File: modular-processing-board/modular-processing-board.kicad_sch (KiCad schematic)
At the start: 0 parts

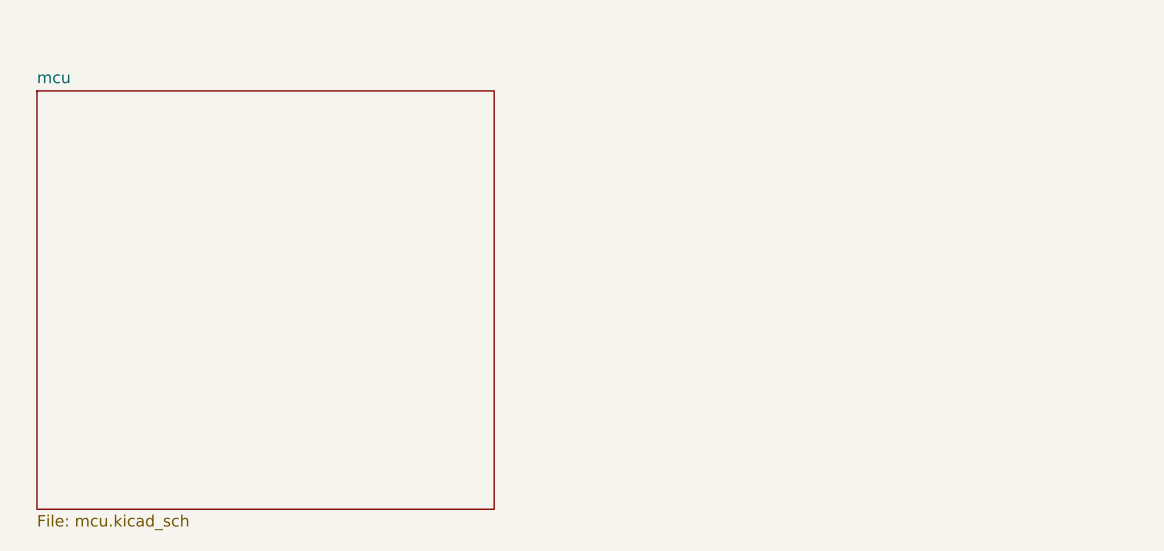
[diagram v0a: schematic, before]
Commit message: research on best communication interfaces, added sdram
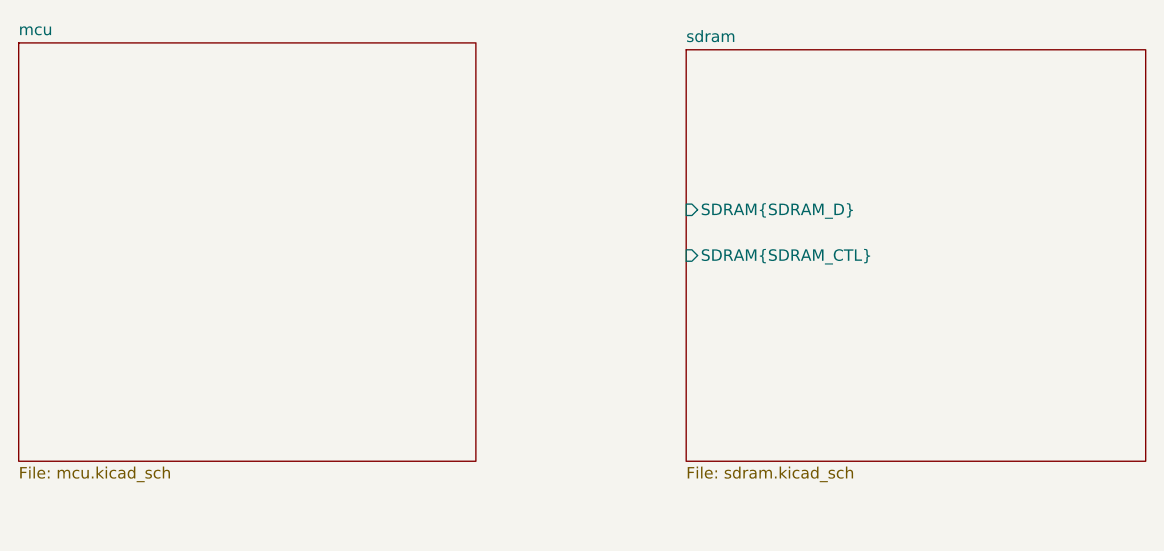
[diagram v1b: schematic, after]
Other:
- added sheet sdram (sdram.kicad_sch)
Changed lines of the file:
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@@
 	(paper "A4")
 	(sheet
-		(at 51.308 64.262)
+		(at 49.276 58.928)
 		(size 50.8 46.482)
 		(exclude_from_sim no)
@@
 		)
 		(property "Sheetname" "mcu"
-			(at 51.308 63.5504 0)
+			(at 49.276 58.2164 0)
 			(effects
 				(font
@@
 		)
 		(property "Sheetfile" "mcu.kicad_sch"
-			(at 51.308 111.3286 0)
+			(at 49.276 105.9946 0)
 			(effects
 				(font
@@
 				)
 			)
+		)
+	)
+	(sheet
+		(at 123.444 59.69)
+		(size 51.054 45.72)
+		(exclude_from_sim no)
+		(in_bom yes)
+		(on_board yes)
+		(dnp no)
+		(fields_autoplaced yes)
+		(stroke
+			(width 0.1524)
+			(type solid)
+		)
+		(fill
+			(color 0 0 0 0.0000)
+		)
+		(property "Sheetname" "sdram"
+			(at 123.444 58.9784 0)
+			(effects
+				(font
+					(size 1.27 1.27)
+				)
+				(justify left bottom)
+			)
+		)
+		(property "Sheetfile" "sdram.kicad_sch"
+			(at 123.444 105.9946 0)
+			(effects
+				(font
+					(size 1.27 1.27)
+				)
+				(justify left top)
+			)
+		)
+		(pin "SDRAM{SDRAM_D}" input
+			(at 123.444 77.47 180)
+			(effects
+				(font
+					(size 1.27 1.27)
+				)
+				(justify left)
+			)
+		)
+		(pin "SDRAM{SDRAM_CTL}" input
+			(at 123.444 82.55 180)
+			(effects
+				(font
+					(size 1.27 1.27)
+				)
+				(justify left)
+			)
+		)
+		(instances
+			(project "modular-processing-board"
+				(path "/73b5a92f-908b-4f97-a96c-14ee20a7f293"
+					(page "3")
+				)
+			)

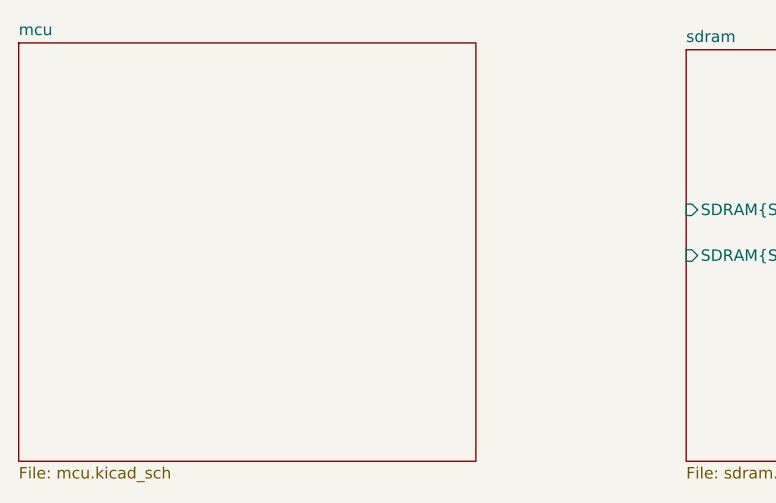
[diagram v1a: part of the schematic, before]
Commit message: basicsic pinout/component selection done, added SDRAM pins (next) Add parallel pins, add connections to pinheaders
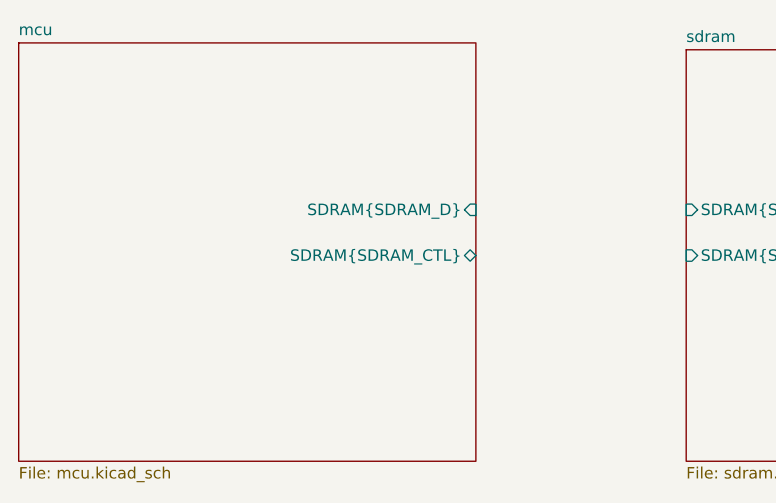
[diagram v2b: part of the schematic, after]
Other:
- sheet mcu ports: added SDRAM{SDRAM_CTL}, SDRAM{SDRAM_D}; removed none
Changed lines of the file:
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@@
+			)
+		)
+		(pin "SDRAM{SDRAM_CTL}" bidirectional
+			(at 100.076 82.55 0)
+			(effects
+				(font
+					(size 1.27 1.27)
+				)
+				(justify right)
+			)
+		)
+		(pin "SDRAM{SDRAM_D}" input
+			(at 100.076 77.47 0)
+			(effects
+				(font
+					(size 1.27 1.27)
+				)
+				(justify right)
 			)
 		)

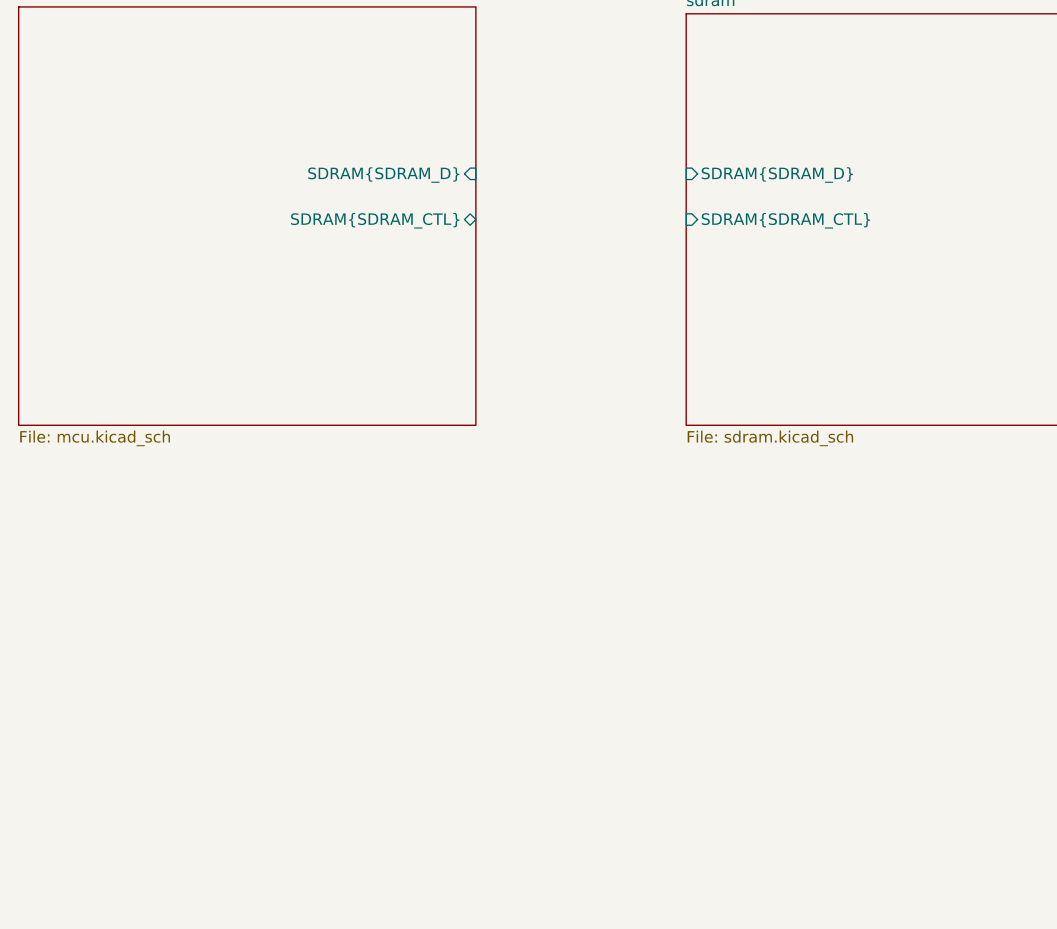
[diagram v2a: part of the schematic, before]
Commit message: added parallel slave bus, SWO, USB (next) add small PSU for CPU-board, add ethernet PHY, add correct USB connector
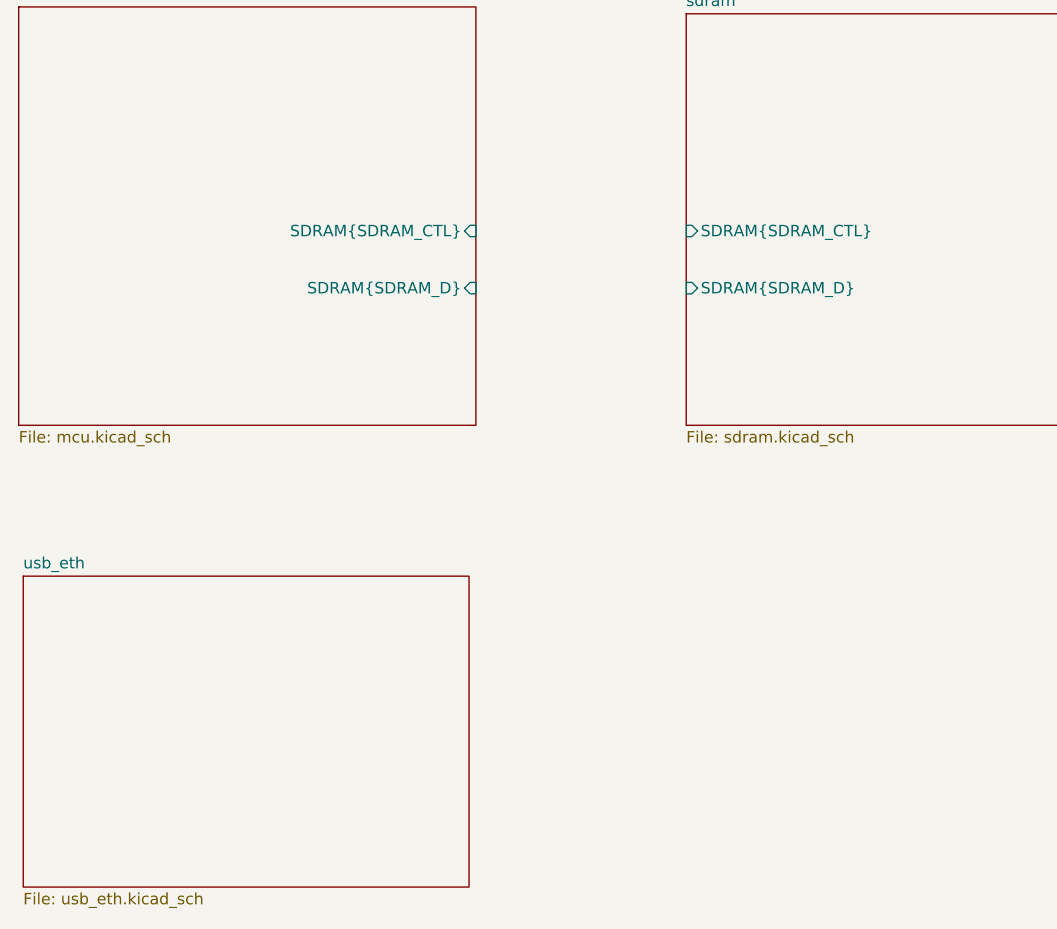
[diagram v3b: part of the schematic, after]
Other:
- added sheet usb_eth (usb_eth.kicad_sch)
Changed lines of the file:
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@@
 			)
 		)
-		(pin "SDRAM{SDRAM_CTL}" bidirectional
-			(at 100.076 82.55 0)
+		(pin "SDRAM{SDRAM_D}" input
+			(at 100.076 90.17 0)
 			(effects
 				(font
@@
 			)
 		)
-		(pin "SDRAM{SDRAM_D}" input
-			(at 100.076 77.47 0)
+		(pin "SDRAM{SDRAM_CTL}" input
+			(at 100.076 83.82 0)
 			(effects
 				(font
@@
 				(path "/73b5a92f-908b-4f97-a96c-14ee20a7f293"
 					(page "2")
+				)
+			)
+		)
+	)
+	(sheet
+		(at 49.784 122.174)
+		(size 49.53 34.544)
+		(exclude_from_sim no)
+		(in_bom yes)
+		(on_board yes)
+		(dnp no)
+		(fields_autoplaced yes)
+		(stroke
+			(width 0.1524)
+			(type solid)
+		)
+		(fill
+			(color 0 0 0 0.0000)
+		)
+		(property "Sheetname" "usb_eth"
+			(at 49.784 121.4624 0)
+			(effects
+				(font
+					(size 1.27 1.27)
+				)
+				(justify left bottom)
+			)
+		)
+		(property "Sheetfile" "usb_eth.kicad_sch"
+			(at 49.784 157.3026 0)
+			(effects
+				(font
+					(size 1.27 1.27)
+				)
+				(justify left top)
+			)
+		)
+		(instances
+			(project "modular-processing-board"
+				(path "/73b5a92f-908b-4f97-a96c-14ee20a7f293"
+					(page "4")
 				)
 			)
@@
 		)
 		(pin "SDRAM{SDRAM_D}" input
-			(at 123.444 77.47 180)
+			(at 123.444 90.17 180)
 			(effects
 				(font
@@
 		)
 		(pin "SDRAM{SDRAM_CTL}" input
-			(at 123.444 82.55 180)
+			(at 123.444 83.82 180)
 			(effects
 				(font

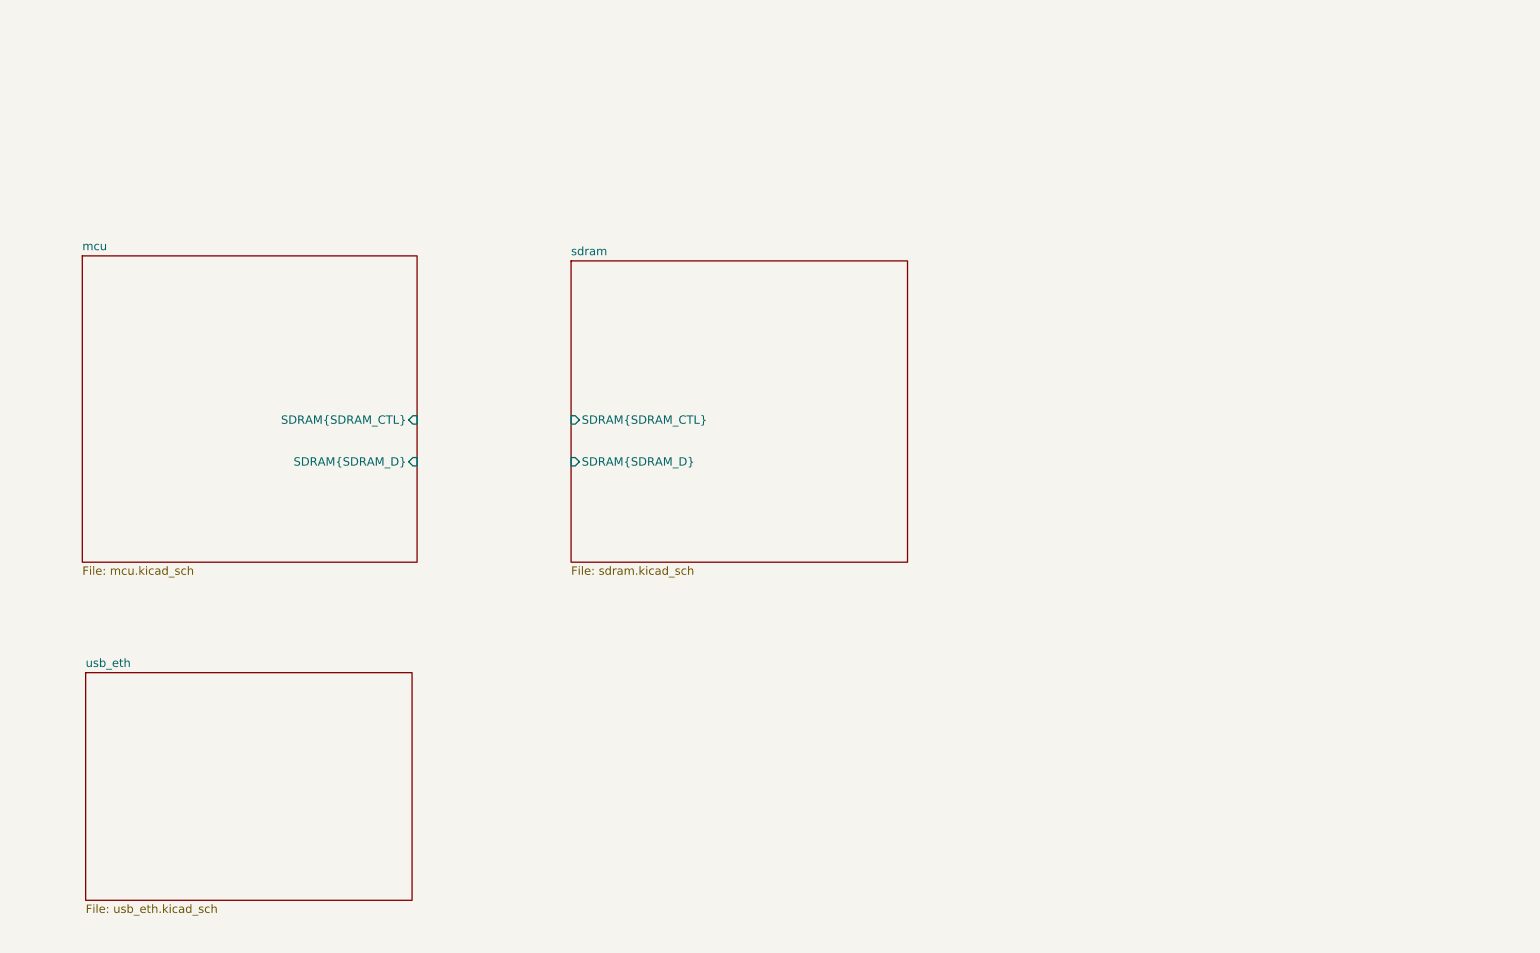
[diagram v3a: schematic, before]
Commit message: added ESD protection,  USB connector, SD-CARD, decoupling caps (next) add appropriate VREF, COAX for ADC, board2board connectors and connect wiring
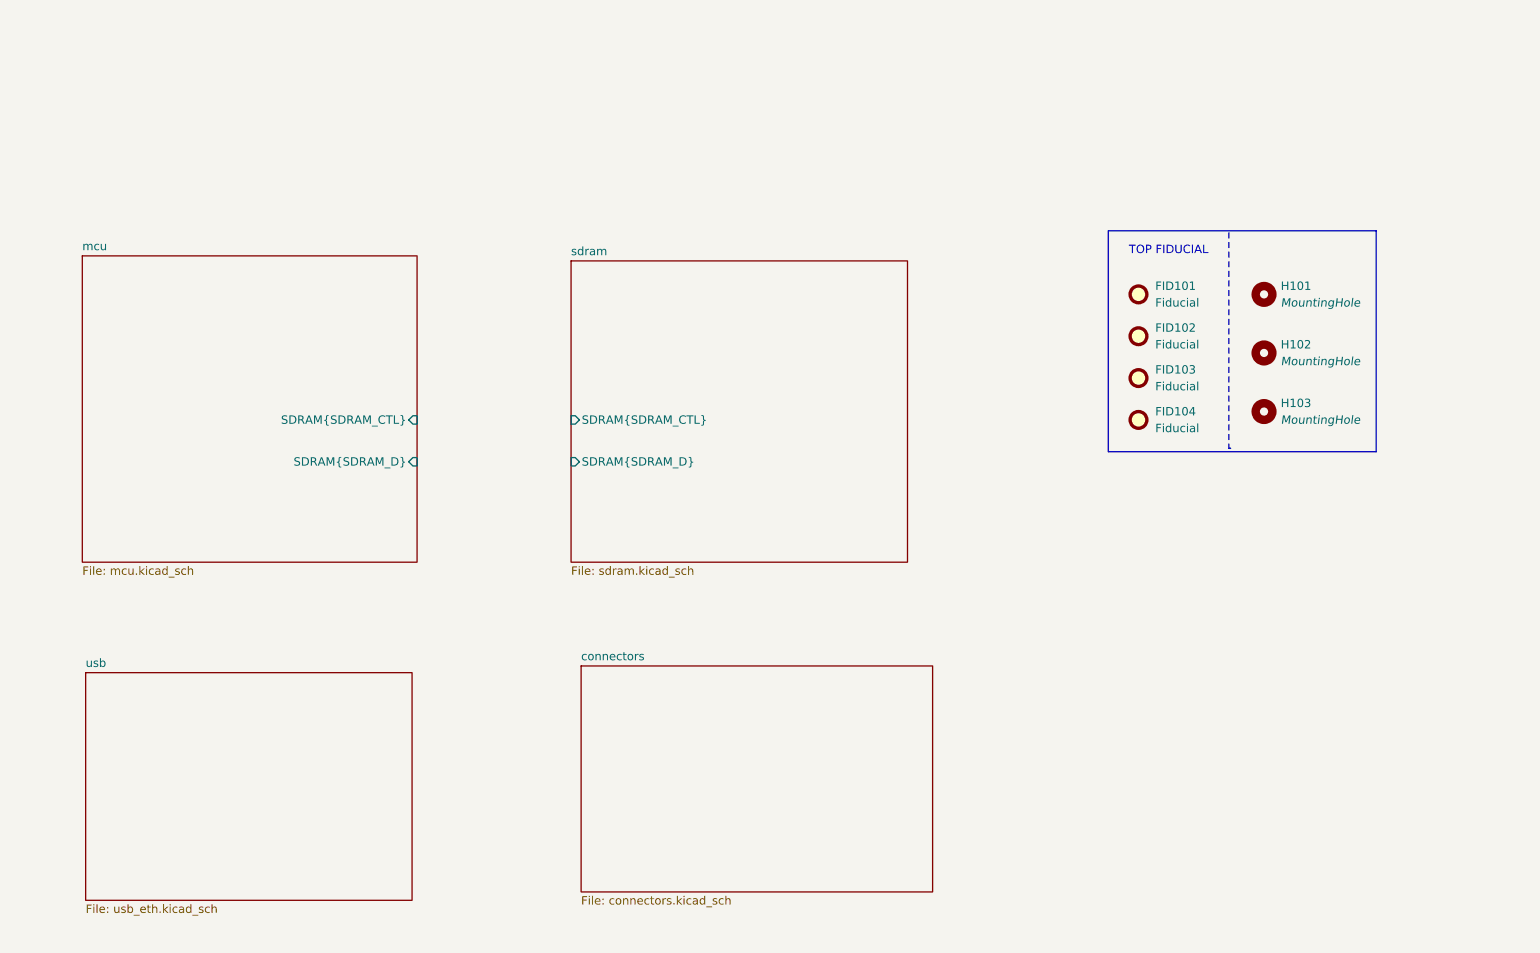
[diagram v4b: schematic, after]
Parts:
- added FID101, FID102, FID103, FID104: Fiducial, Fiducial:Fiducial_1mm_Mask2mm, symbol Mechanical:Fiducial
- added H101, H102, H103: MountingHole, MountingHole:ToolingHole_1.152mm, symbol Mechanical:MountingHole
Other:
- sheet usb_eth renamed usb
- added sheet connectors (connectors.kicad_sch)
- note added: "TOP FIDUCIAL"

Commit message: Finished basic HW (next) Fix-up all labeling, then start laying out
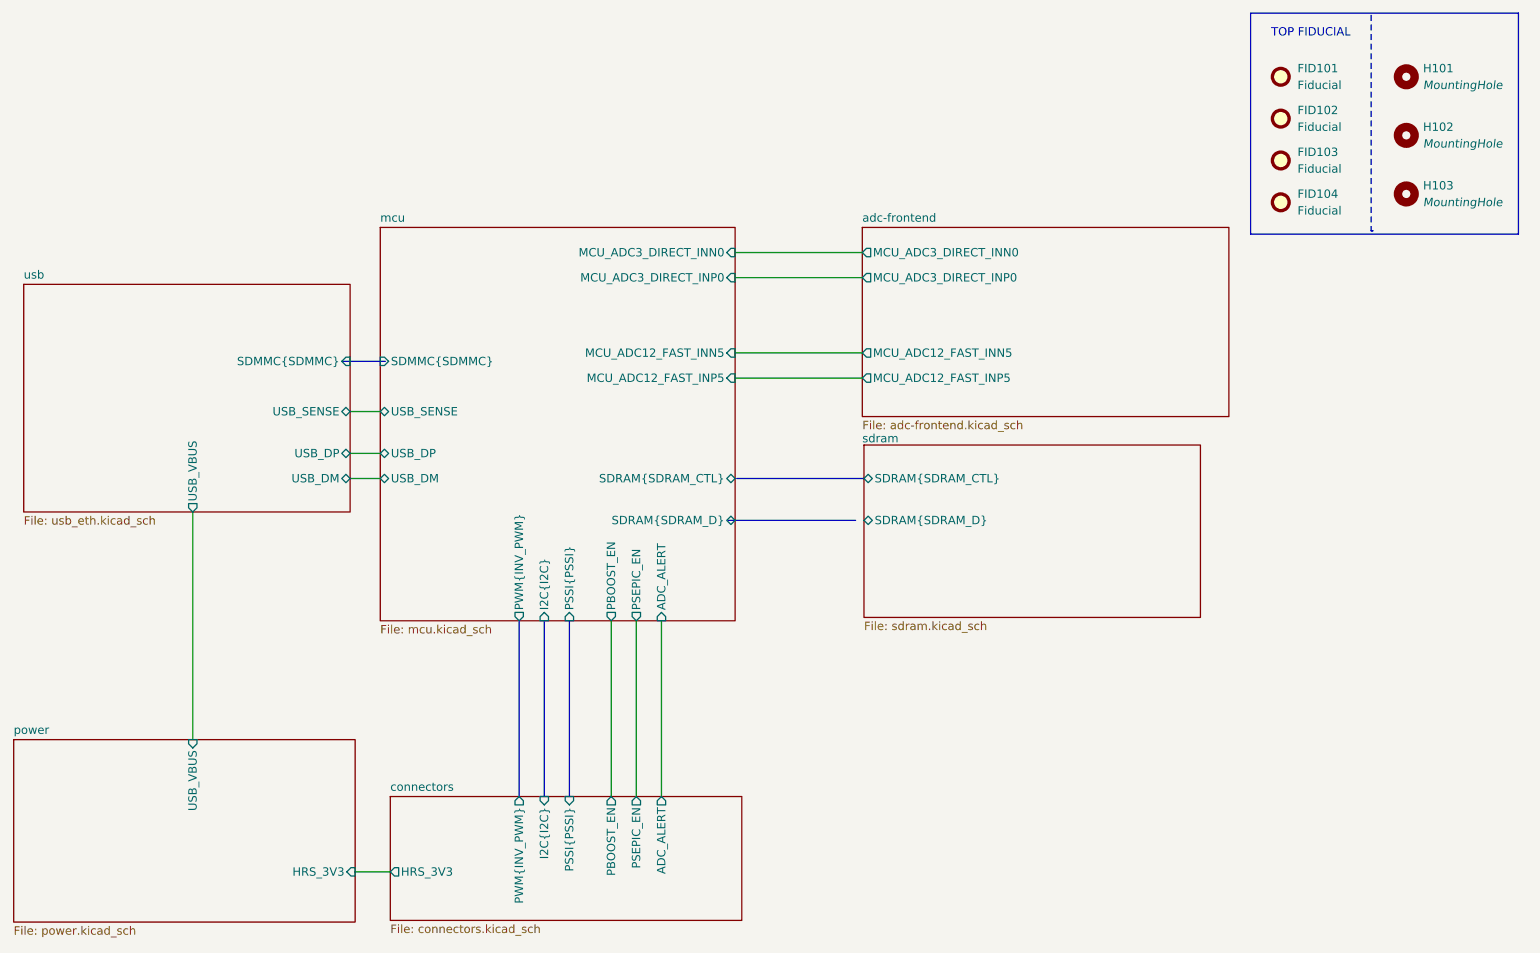
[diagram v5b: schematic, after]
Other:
- added sheet adc-frontend (adc-frontend.kicad_sch)
- added sheet power (power.kicad_sch)
- sheet connectors ports: added ADC_ALERT, HRS_3V3, I2C{I2C}, PBOOST_EN, PSEPIC_EN, PSSI{PSSI}, PWM{INV_PWM}; removed none
- sheet mcu ports: added ADC_ALERT, I2C{I2C}, MCU_ADC12_FAST_INN5, MCU_ADC12_FAST_INP5, MCU_ADC3_DIRECT_INN0, MCU_ADC3_DIRECT_INP0, PBOOST_EN, PSEPIC_EN, PSSI{PSSI}, PWM{INV_PWM}, SDMMC{SDMMC}, USB_DM, USB_DP, USB_SENSE; removed none
- sheet usb ports: added SDMMC{SDMMC}, USB_DM, USB_DP, USB_SENSE, USB_VBUS; removed none
- moved on the sheet: FID101, FID102, FID103, FID104, H101, H102, H103
